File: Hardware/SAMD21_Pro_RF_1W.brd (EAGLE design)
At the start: 53.3 x 40.6 mm, 134 parts, among them J10 AVR_SPI_PROG_3X2TESTPOINTS, J12 5.5x2.1mm Barrel, J13 U.FL, J7 PTH, J9 External On/Off, Q1 310mA/60V/1.6Ω, U1 MCP73831, U3 3.3V, U4 ATSAMD21G, U5 4MB Flash, U6 E19-915MS1W, U7 ADJ5, U8 TXB0108DQSR, Y1 32.768kHz

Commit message: Finalizing things
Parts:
- moved U$26 121.9 mm to (-34.3, -14.0), flipped to the top
- moved FRAME2 81.3 mm to (-14.0, -12.7), flipped to the top
- moved U$29 51.6 mm to (52.5, 34.7), flipped to the top
- moved U$40 51.3 mm to (52.3, 0.38), flipped to the top
- moved FD2 50.8 mm to (52.1, 36.8), flipped to the bottom
- moved J7 50.8 mm to (1.27, 3.81), flipped to the top
- moved U6 50.8 mm to (1.27, 7.62), flipped to the bottom
- moved U$56 48.8 mm to (51.1, 0.89), flipped to the bottom
- moved U$54 48.5 mm to (50.9, 39.8), flipped to the bottom
- moved J13 48.3 mm to (50.8, 31.1), flipped to the top
- moved LOGO1 48.3 mm to (2.54, 36.7), flipped to the bottom
- moved U$35 48.3 mm to (50.8, 33.8), flipped to the bottom
- moved U$61 48.3 mm to (2.54, 36.7), flipped to the top
- moved U$81 47.8 mm to (50.5, 11.4), flipped to the top
- moved U$32 46.0 mm to (3.68, 5.59), flipped to the bottom
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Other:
- outline, holes or cut-outs redrawn

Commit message: x02
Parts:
- removed FRAME2: FRAME-LEDGER, SparkFun-Aesthetics:CREATIVE_COMMONS
- removed J15, J2: (no value), SparkFun-Connectors:1X04_1MM_RA
- removed LED1: RED, SparkFun-LED:LED-0603
- removed R15: 240, SparkFun-Resistors:0603
- removed R16: 10k, SparkFun-Resistors:0603
- removed S3: (no value), SparkFun-Switches:TACTILE_SWITCH_SMD_RIGHT_ANGLE
- removed U7: ADJ5, SparkFun-IC-Power:SOT223
- removed U8: TXB0108DQSR, SparkFun-IC-Comms:UFDFN-20
- added D2: Green, SparkFun-LED:LED-0603
- added FRAME1: FRAME-LEDGER, SparkFun-Aesthetics:CREATIVE_COMMONS
- added J14: CORTEX_DEBUG_PTH, SparkFun-Connectors:2X5-PTH-1.27MM
- added Q2: 310mA/60V/1.6Ω, SparkFun-DiscreteSemi:SOT323
- added R11: 10k, SparkFun-Resistors:0603
- added R3, R4: 1k, SparkFun-Resistors:0603
- added S2: Power, SparkFun-Switches:SWITCH_SPST_SMD_A
- added U$58: (no value), SparkX:SPARKX-MEDIUM
- added U$59: (no value), buzzard_labels:D130
- added U$60: (no value), buzzard_labels:SCK18
- added U2: 3.3V, SparkFun-IC-Power:SOT23-5
- C1: value 10uF -> 15pF; device SparkFun-Capacitors:EIA3216 -> SparkFun-Capacitors:0603
- C10: value 0.1uF -> 10uF; device SparkFun-Capacitors:0603 -> SparkFun-Capacitors:EIA3216
- C11, C14: value 0.1uF -> 1.0uF
- C12: value 1.0uF -> 10uF; device SparkFun-Capacitors:0603 -> SparkFun-Capacitors:EIA3216
- C13, C7: value 10uF -> 0.1uF; device SparkFun-Capacitors:EIA3216 -> SparkFun-Capacitors:0603
- C3: value 15pF -> 0.1uF
- C5: value 1.0uF -> 0.1uF
- C8: value 0.1uF -> 4.7uF
- C9: value 4.7uF -> 10uF; device SparkFun-Capacitors:0603 -> SparkFun-Capacitors:EIA3216
- D1: value Green -> Yellow
- D3: value 3A/10V/300mV -> BLUE; device SAMD21_ProRF_1W:SOD-323 -> SparkFun-LED:LED-0603
- D4: value BLUE -> 3A/10V/300mV; device SparkFun-LED:LED-0603 -> SAMD21_ProRF_1W:SOD-323
- D6: value Yellow -> RED
- J10: value AVR_SPI_PROG_3X2TESTPOINTS -> (none); device SparkFun-Connectors:2X3_TEST_POINTS -> SparkFun-Connectors:1X10_NO_SILK
- J11: device SparkFun-Connectors:1X09_NO_SILK -> SparkFun-Connectors:1X04_1MM_RA
- J12: value 5.5x2.1mm Barrel -> (none); device SparkFun-Connectors:POWER_JACK_SMD -> SparkFun-Connectors:1X01_NO_SILK
- J13: value U.FL -> (none); device SparkFun-Connectors:U.FL -> SparkFun-Connectors:1X04_1MM_RA
- J3: value (none) -> PTH; device SparkFun-Connectors:1X10_NO_SILK -> SparkFun-Connectors:1X02_NO_SILK
- J4: device SparkFun-Connectors:1X01_NO_SILK -> SparkFun-Connectors:1X02_NO_SILK
- J5: value (none) -> 5.5x2.1mm Barrel; device SparkFun-Connectors:1X09_NO_SILK -> SparkFun-Connectors:POWER_JACK_SMD
- J7: value PTH -> (none); device SparkFun-Connectors:1X02_NO_SILK -> SparkFun-Connectors:1X09_NO_SILK
- J8: value (none) -> External On/Off
- J9: value External On/Off -> (none); device SparkFun-Connectors:1X02_NO_SILK -> SparkFun-Connectors:1X09_NO_SILK
- R10, R7, R9: value 1k -> 10k
- R13: value 1k -> 2.2k
- R14: value 750 -> 2.2k
- R2, R8: value 10k -> 1k
- R5: value 2.2k -> 240
- R6: value 10k -> 750
- S1: value Power -> MOMENTARY-SWITCH-SPST-SMD-5.2-REDUNDANT; device SparkFun-Switches:SWITCH_SPST_SMD_A -> SparkFun-Switches:TACTILE_SWITCH_SMD_5.2MM
- U$10: device buzzard_labels (25):SCK10 -> buzzard_labels:MISO4
- U$18: device D2:D20 -> buzzard_labels:SCK5
- U$2: device D2:D20 -> buzzard_labels:MISO4
- U$20: device D3:D30 -> buzzard_labels:MOSI3
- U$21: device D3:D30 -> buzzard_labels:SPI11
- U$22: device D4:D40 -> buzzard_labels:MISO17
- U$26: value SPECIAL_INSTRUCTIONS-ORDERING -> (none); device SparkFun-Aesthetics:ORDERING_INSTRUCTIONS -> buzzard_labels:SAMD21_PRORF_1W5
- U$31: device D4:D40 -> buzzard_labels:MOSI16
- U$36: device buzzard_labels (25):RST2 -> buzzard_labels:OFF#ON1
- U$39: device buzzard_labels (28):ON#OFF0 -> buzzard_labels:SCK5
- U$65: device buzzard_labels (9):CHG1 -> buzzard_labels:SPI11
- U$8: device buzzard_labels (25):MISO8 -> buzzard_labels:SPI2
- U$9: device buzzard_labels (25):MOSI9 -> buzzard_labels:MOSI3
- U1: value MCP73831 -> ATSAMD21G; device SparkFun-IC-Power:SOT23-5 -> temp:QFN-48_NO_EXPOSED_PAD
- U3: value 3.3V -> ADJ5; device SparkFun-IC-Power:SOT23-5 -> SparkFun-IC-Power:SOT223
- U4: value ATSAMD21G -> 4MB Flash; device temp:QFN-48_NO_EXPOSED_PAD -> SparkFun-IC-Memory:SO08
- U5: value 4MB Flash -> E19-915MS1W; device SparkFun-IC-Memory:SO08 -> SAMD21_ProRF_1W:E19-915MS1W
- U6: value E19-915MS1W -> TXB0108DQSR; device SAMD21_ProRF_1W:E19-915MS1W -> SparkFun-IC-Comms:UFDFN-20
- moved U$26 56.9 mm to (2.79, 29.2), turned to 270 degrees
- moved S1 52.7 mm to (49.5, 34.8), flipped to the bottom, turned to 270 degrees
- moved J13 52.6 mm to (5.08, 5.08), flipped to the bottom, turned to 0 degrees
- moved U$29 51.6 mm to (0.89, 34.7), flipped to the bottom
- moved U$40 51.3 mm to (1.02, 0.38), flipped to the bottom
- moved U$56 48.8 mm to (2.29, 0.89), flipped to the top
- moved U$54 48.5 mm to (2.41, 39.8), flipped to the top
- moved U$35 48.3 mm to (2.54, 33.8), flipped to the top
- moved U$36 47.8 mm to (42.8, 4.70), flipped to the top
- moved U$81 47.8 mm to (2.79, 11.4), flipped to the bottom
- moved U$28 46.8 mm to (52.7, 33.3), flipped to the bottom, turned to 90 degrees
- moved U$32 46.0 mm to (49.7, 5.59), flipped to the top
- moved J7 45.8 mm to (33.0, 36.8), flipped to the bottom, turned to 0 degrees
- moved U$70 45.5 mm to (3.91, 6.92), flipped to the bottom
- moved U$72 45.5 mm to (3.91, 8.45), flipped to the bottom
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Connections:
- removed net CHARGE_STAT: R9.1, U1.1
- removed net D2: J3.6, U4.23
- removed net D3: J3.5, U4.14
- removed net D4: J3.4, U4.13
- removed net E19_RST: U4.26, U6.P$8
- removed net N$11: R5.1, U1.5
- removed net N$8: D4.C, R9.2
- removed net N$9: J9.2, S1.1
- removed net VBATT_LVL: R1.1, R2.2, U4.47
- new net !E19_RST: Q1.2, R9.1, U1.22
- new net !E19_RST5V: Q1.3, R11.1, U5.P$8
- new net D13: R4.2, U1.26
- new net EEPROM_MISO: J6.6, U1.23, U4.2
- new net EEPROM_MOSI: J6.4, U1.13, U4.5
- new net EEPROM_SCLK: J6.5, U1.14, U4.6
- new net N$3: D3.A, R4.1
- net !E19_CS: now also Q2.2, R10.1, U1.28; no longer Q1.2, R12.1, U4.28
- net !E19_CS5V: now also Q2.3, R12.1, U5.P$15; no longer Q1.3, R16.1, U6.P$15
- net !RST: now also J14.10, J6.8, R1.1, S1.3, S1.4, U1.40; no longer J10.5, J3.8, R6.1, S3.1, U4.40
- net 3.3V: now also C10.+, C11.1, C13.2, C5.2, D2.A, J11.2, J13.2, J14.1, J6.2, Q2.1, R1.2, R10.2, R14.2, R7.2, R9.2, U1.17, U1.36, U1.43, U1.44, U2.5, U4.3, U4.7, U4.8, U6.5, U6.6; no longer C10.2, C12.1, C13.+, C14.2, D6.A, J10.2, J15.2, J2.2, J3.2, R12.2, R6.2, U3.5, U4.17, U4.36, U4.43, U4.44, U5.3, U5.7, U5.8, U8.5, U8.6
- net 5V: now also C12.+, C14.1, C15.2, D4.C, R11.2, R12.2, U2.1, U2.3, U5.P$11, U6.16; no longer C5.1, C7.+, C8.2, D3.C, R16.2, U3.1, U3.3, U6.P$11, U8.16
- net A0: now also J7.9, U1.3; no longer J11.9, U4.3
- net A1: now also J7.8, U1.7; no longer J11.8, U4.7
- net A2: now also J7.7, U1.8; no longer J11.7, U4.8
- net A3: now also J7.6, U1.9; no longer J11.6, U4.9
- net A4: now also J7.5, U1.10; no longer J11.5, U4.10
- net ANT: now also J12.1, U5.P$19; no longer J13.FEED, J4.1, U6.P$19
- net D+: now also U1.34; no longer U4.34
- net D-: now also U1.33; no longer U4.33
- net D10: now also U1.27, U6.9; no longer U4.27, U8.9
- net D11: now also U1.25, U6.10; no longer U4.25, U8.10
- net D5: now also J6.7, U1.24; no longer J3.7, U4.24
- net D8_!FLASH_CS: now also R7.1, U1.11, U4.1; no longer R8.1, U4.11, U5.1
- net D9: now also J6.3, U1.12; no longer J3.3, U4.12
- net DIO05V: now also U5.P$7, U6.13; no longer U6.P$7, U8.13
- net DIO15V: now also U5.P$6, U6.12; no longer U6.P$6, U8.12
- net DIO25V: now also U5.P$5, U6.11; no longer U6.P$5, U8.11
- net E19_INT: now also U1.29, U6.8; no longer U4.29, U8.8
- net E19_RXEN: now also U1.38, U6.7; no longer U4.38, U8.7
- net E19_RXEN5V: now also U5.P$17, U6.14; no longer U6.P$17, U8.14
- net E19_TXEN: now also U1.37, U6.4; no longer U4.37, U8.4
- net E19_TXEN5V: now also U5.P$16, U6.17; no longer U6.P$16, U8.17
- net GND: now also C1.1, C10.-, C11.2, C12.-, C13.1, C14.2, C5.1, C7.1, C8.2, C9.-, D3.C, D6.C, J10.1, J10.10, J10.2, J10.3, J10.4, J10.5, J10.7, J10.8, J10.9, J14.3, J14.5, J3.1, J4.1, J5.GND, J5.P$4, J9.1, J9.2, J9.3, J9.4, J9.5, J9.6, J9.7, J9.8, J9.9, R6.1, S1.1, S1.2, U1.18, U1.35, U1.42, U1.5, U2.2, U4.4, U5.P$1, U5.P$10, U5.P$18, U5.P$20, U5.P$21, U5.P$22, U5.P$9, U6.15; no longer C1.-, C10.1, C11.1, C12.2, C13.-, C14.1, C5.2, C7.-, C8.1, C9.2, J12.GND, J12.P$4, J13.2, J15.1, J2.1, J5.1, J5.2, J5.3, J5.4, J5.5, J5.6, J5.7, J5.8, J5.9, J6.1, J6.10, J6.2, J6.3, J6.4, J6.5, J6.6, J6.7, J6.8, J6.9, J8.1, LED1.C, R14.1, R2.1, R5.2, S3.2, U1.2, U3.2, U4.18, U4.35, U4.42, U4.5, U5.4, U6.P$1, U6.P$10, U6.P$18, U6.P$20, U6.P$21, U6.P$22, U6.P$9, U8.15
- net MISO: now also J14.6, J7.2, U1.21, U6.2; no longer J10.1, J11.2, U4.21, U5.2, U8.2
- net MISO5V: now also U5.P$13, U6.19; no longer U6.P$13, U8.19
- net MOSI: now also J7.3, U1.19, U6.3; no longer J11.3, U4.19, U5.5, U8.3
- net MOSI5V: now also U5.P$14, U6.18; no longer U6.P$14, U8.18
- net N$1: now also D1.C, R2.2; no longer D6.C, R10.2
- net N$12: now also D4.A; no longer D3.A
- net N$13: now also R5.1, R6.2, U3.1; no longer R14.2, R15.1, U7.1
- net N$14: now also R5.2, U3.2, U3.4; no longer R15.2, U7.2, U7.4
- net N$2: now also D2.C, R3.2; no longer D1.C, R7.2
- net N$38: now also D6.A, R8.1; no longer LED1.A, R13.1
- net N$6: now also C1.2, U1.1; no longer C2.2, U4.1
- net N$7: now also C2.2, U1.2; no longer C3.2, U4.2
- net RAW: now also J6.1, J8.1, S2.2, U3.3; no longer J3.1, J9.1, S1.2, U7.3
- net RXI: now also J6.10, U1.16; no longer J3.10, U4.16
- net RX_LED: now also R2.1, U1.48; no longer R10.1, U4.48
- net SCK: now also J7.4, U1.20, U6.1; no longer J11.4, U4.20, U5.6, U8.1
- net SCK5V: now also U5.P$12, U6.20; no longer U6.P$12, U8.20
- net SCL: now also J11.4, J13.4, R14.1, U1.32; no longer J15.4, J2.4, U4.32
- net SDA: now also J11.3, J13.3, R13.1, U1.31; no longer J15.3, J2.3, U4.31
- net SWDCLK: now also J14.4, U1.45; no longer J10.3, U4.45
- net SWDIO: now also J14.2, U1.46; no longer J10.4, U4.46
- net TXO: now also J6.9, U1.15; no longer J3.9, U4.15
- net TX_LED: now also R3.1, U1.39; no longer R7.1, U4.39
- net USB_VCC: now also C3.2, C8.1, J4.2; no longer C11.2, C9.1, D4.A, J8.2, U1.4
- net VBATT: now also C9.+, J3.2, J5.VIN0, J8.2, S2.3; no longer C1.+, J12.VIN0, J7.2, R1.2, S1.3, U1.3
- net VDDANA: now also C7.2, U1.6; no longer C15.2, U4.6
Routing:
- net CHARGE_STAT: track 74.0 -> 0.00 mm, vias 4 -> 0
- net VBATT_LVL: track 52.4 -> 0.00 mm, vias 6 -> 0
- net USB_VCC: track 100.4 -> 53.3 mm, vias 6 -> 4
- net !E19_RST5V: track 0.00 -> 45.1 mm, vias 0 -> 3
- net E19_RST: track 32.0 -> 0.00 mm, vias 1 -> 0
- net EEPROM_MISO: track 0.00 -> 30.0 mm, vias 0 -> 2
- net MOSI: track 71.8 -> 50.4 mm, vias 4 -> 2
- net EEPROM_SCLK: track 0.00 -> 20.8 mm, vias 0 -> 1
- net EEPROM_MOSI: track 0.00 -> 19.3 mm, vias 0 -> 1
- net !E19_RST: track 0.00 -> 18.0 mm, vias 0 -> 2
- net SCK: track 69.6 -> 52.3 mm, vias 7 -> 4
- net 3.3V: track 187.3 -> 204.5 mm
- net D4: track 14.2 -> 0.00 mm, vias 1 -> 0
- net D13: track 0.00 -> 13.8 mm, vias 0 -> 2
- net D3: track 13.5 -> 0.00 mm, vias 1 -> 0
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- removed copper zone on layer 16, net ANT
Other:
- outline, holes or cut-outs redrawn
- board text added: "x02"
- board text removed: "0.8mm Board Thickness"
- board text removed: "x01"

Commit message: x02 ready for order
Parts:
- removed LOGO1: OSHW-LOGOMINI, SparkFun-Aesthetics:OSHW-LOGO-MINI
- removed U$29, U$40, U$54, U$56: (no value), Labels:QWIIC-TEXT-04
- added U$64, U$67: (no value), Labels:QWIIC_COPYRIGHT_SMALL
- U$30: device Labels:QWIIC-LOGO-MEDIUM -> Labels:QWIIC_COPYRIGHT_MEDIUM
- U$34: value SPARKX-LOGO2 -> SPARKX-LOGO4; device SparkX:SPARKX-TINY -> SparkX:SPARKX-MEDIUM
- U$51: device SparkX:SPARKX-MEDIUM -> Labels:QWIIC_COPYRIGHT_MEDIUM
- moved FRAME1 81.3 mm to (-14.0, -12.7), flipped to the top
- moved U$28 52.1 mm to (0.64, 33.3), flipped to the top
- moved FD1 50.8 mm to (52.1, 36.8), flipped to the bottom
- moved J3 50.8 mm to (1.27, 3.81), flipped to the top
- moved U5 50.8 mm to (1.27, 7.62), flipped to the bottom
- moved FD2 49.8 mm to (1.78, 2.29), flipped to the top
- moved FD3 49.8 mm to (1.78, 2.29), flipped to the bottom
- moved U$35 48.3 mm to (50.8, 33.8), flipped to the bottom
- moved U$26 47.8 mm to (50.5, 29.2), flipped to the bottom
- moved U$81 47.8 mm to (50.5, 11.4), flipped to the top
- moved U$32 46.0 mm to (3.68, 5.59), flipped to the bottom
- moved S1 45.7 mm to (3.81, 34.8), flipped to the top
- moved U$63 45.7 mm to (49.5, 11.5), flipped to the top
- moved U$59 45.6 mm to (49.5, 9.96), flipped to the top
- moved U$70 45.5 mm to (49.4, 6.92), flipped to the top
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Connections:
- net GND: now also J14.9
- net MISO: no longer J14.6
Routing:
- net MISO: track 77.3 -> 53.4 mm, vias 5 -> 2
- net GND: track 133.4 -> 132.6 mm
- net 3.3V: track 204.5 -> 203.9 mm
- added copper zone on layer 16, net ANT
- removed copper zone on layer 1, net ANT
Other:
- outline, holes or cut-outs redrawn

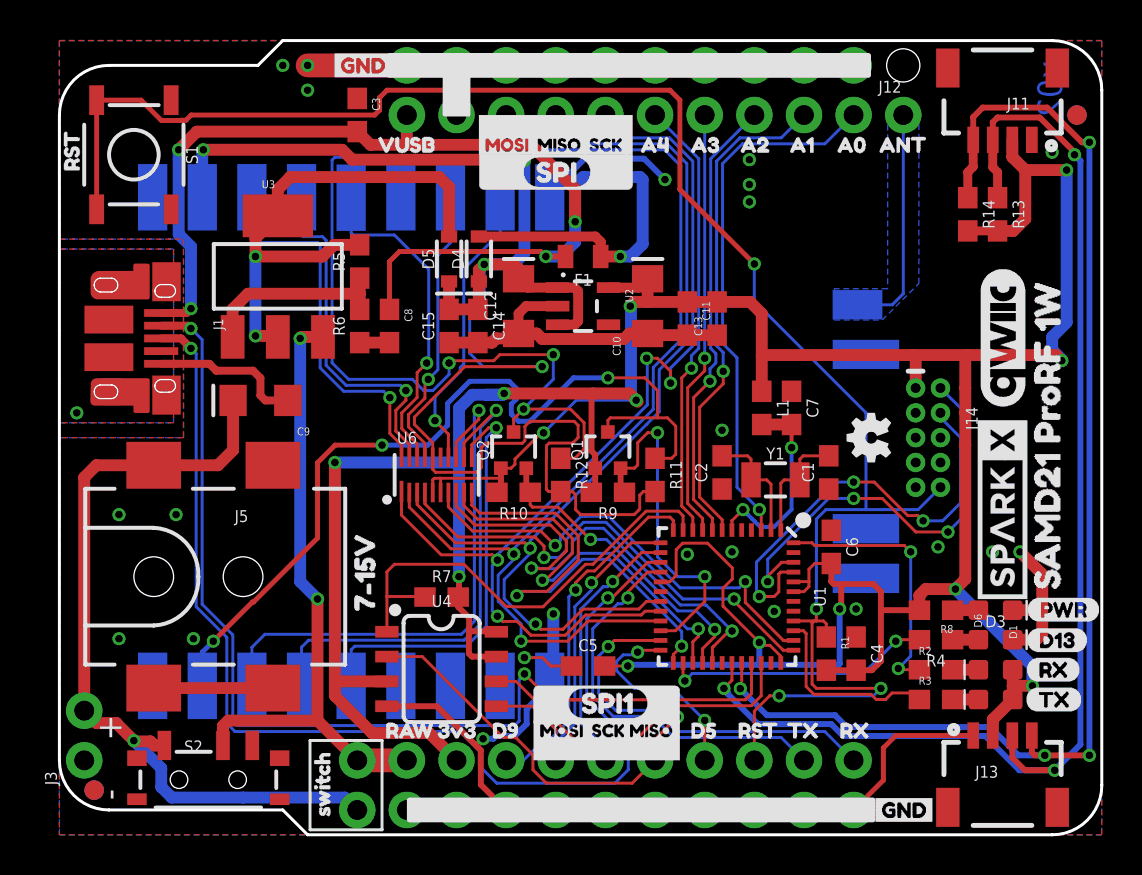
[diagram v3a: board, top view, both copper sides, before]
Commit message: Brought libraries into spec
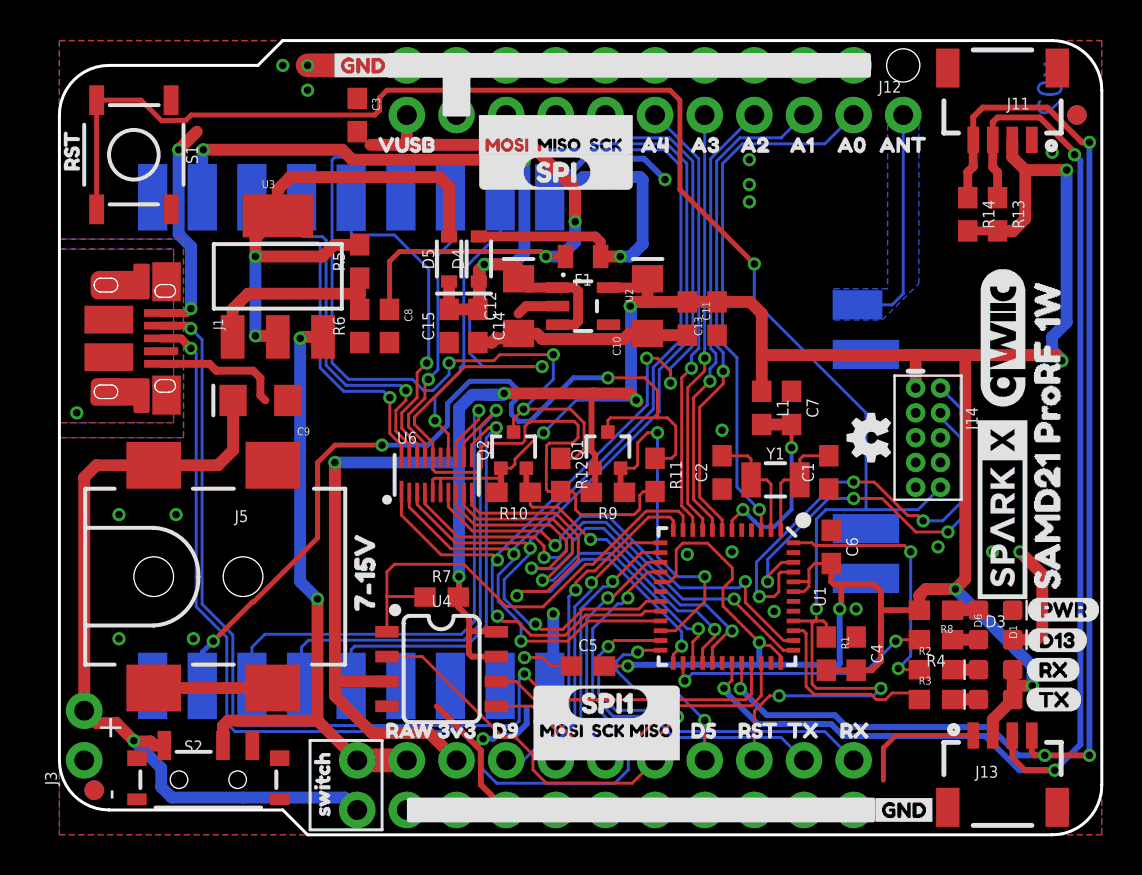
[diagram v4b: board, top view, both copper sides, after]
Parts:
- D4, D5: value 3A/10V/300mV -> 3A/10V/280mV; device SAMD21_ProRF_1W:SOD-323 -> SparkFun-DiscreteSemi:SOD-323
- U1: device temp:QFN-48_NO_EXPOSED_PAD -> SparkFun-IC-Microcontroller:QFN-48_NO_EXPOSED_PAD
- U5: value E19-915MS1W -> (none); device SAMD21_ProRF_1W:E19-915MS1W -> SparkFun-RF:E19-915MS1W
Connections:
- new net V_USB: C3.2
- net USB_VCC: no longer C3.2
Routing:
- net GND: track 132.6 -> 111.6 mm
- net USB_VCC: track 53.3 -> 44.1 mm
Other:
- board text added: "BAT60A"
- board text added: "Ferrite Chip 30 Ohm"
- board text added: "N-ch"
- board text added: "Tall Cap Tactile"

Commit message: Fixes
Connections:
- removed net USB_VCC: C8.1, F1.2, J1.VBUS, J4.2, JP1.2
- net V_USB: now also C8.1, F1.2, J1.VBUS, J4.2, JP1.2
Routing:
- net V_USB: track 0.00 -> 53.3 mm, vias 0 -> 4
- net USB_VCC: track 44.1 -> 0.00 mm, vias 4 -> 0
- net GND: track 111.6 -> 101.4 mm

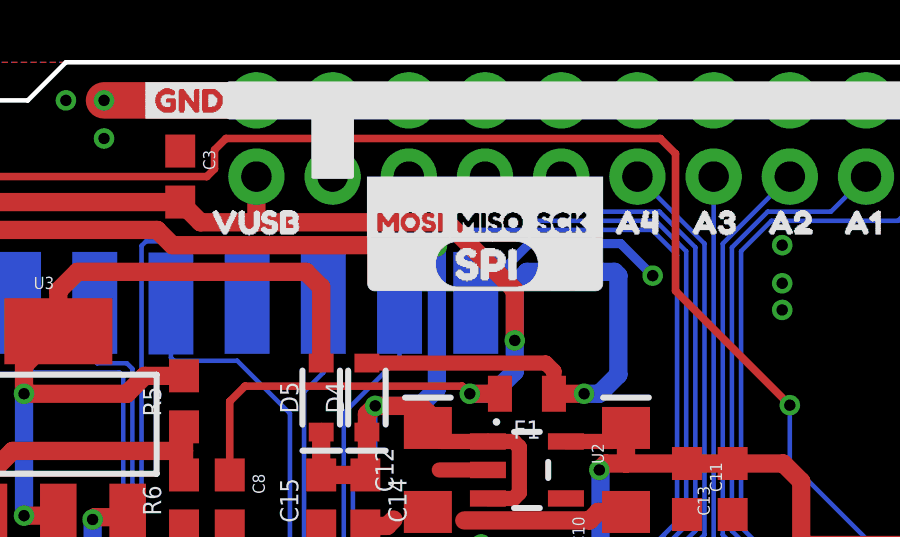
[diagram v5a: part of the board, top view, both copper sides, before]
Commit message: Fixed silkscreen of "SPI" on top side
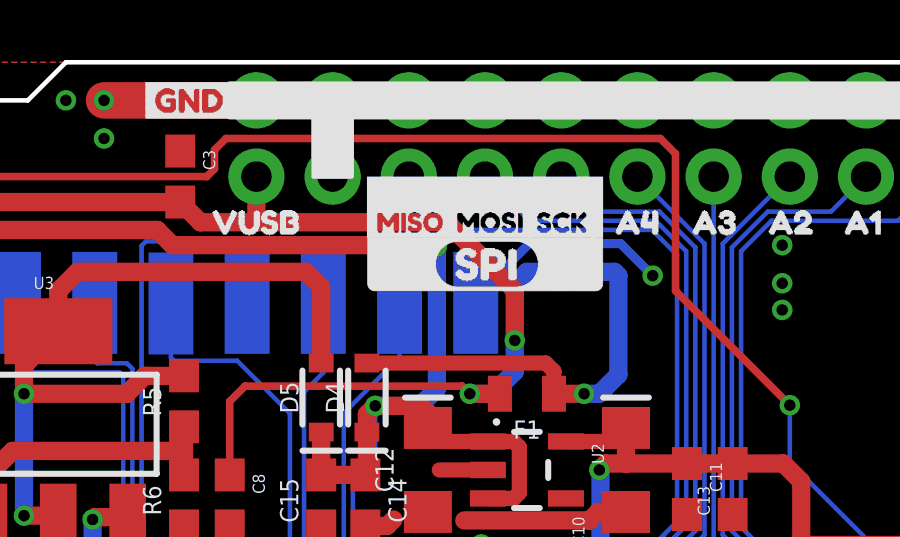
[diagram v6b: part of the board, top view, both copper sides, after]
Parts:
- moved U$10 2.67 mm to (21.2, 35.3)
- moved U$9 2.67 mm to (23.9, 35.3)
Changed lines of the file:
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@@
 <attribute name="VALUE" value="Yellow" x="46.2534" y="13.6525" size="0.508" layer="27" ratio="15" rot="R180"/>
 </element>
-<element name="FRAME1" library="SparkFun-Aesthetics" package="CREATIVE_COMMONS" value="FRAME-LEDGER" x="-13.97" y="-12.7"/>
+<element name="FRAME1" library="SparkFun-Aesthetics" package="CREATIVE_COMMONS" value="FRAME-LEDGER" x="-13.97" y="-12.7">
+<attribute name="DESIGNER" value="" x="-13.97" y="-12.7" size="1.778" layer="27" display="off"/>
+<attribute name="REV" value="" x="-13.97" y="-12.7" size="1.778" layer="27" display="off"/>
+</element>
 <element name="J1" library="SparkFun-Connectors" package="USB-MICROB-PTH-MILL" value="" x="5.207" y="25.4" smashed="yes" rot="R270">
 <attribute name="NAME" x="7.874" y="26.416" size="0.508" layer="25" font="vector" rot="R270"/>
@@
 <element name="F1" library="SparkFun-Fuses" package="0805" value="6V 0.5A" x="26.797" y="29.591" smashed="yes" rot="R180">
 <attribute name="NAME" x="26.797" y="28.702" size="0.6096" layer="25" font="vector" ratio="20" rot="R180" align="bottom-center"/>
-<attribute name="VALUE" x="26.924" y="31.115" size="0.6096" layer="27" font="vector" ratio="20" align="top-center"/>
+<attribute name="PROD_ID" value="13945" x="26.797" y="29.591" size="1.778" layer="27" rot="R180" display="off"/>
+<attribute name="VALUE" value="6V 0.5A" x="26.924" y="31.115" size="0.6096" layer="27" font="vector" ratio="20" align="top-center"/>
 </element>
 <element name="R6" library="SparkFun-Resistors" package="0603" value="750" x="15.367" y="26.035" smashed="yes" rot="R90">
@@
 <element name="U$36" library="buzzard_labels" package="OFF#ON1" value="" x="10.541" y="4.699" rot="MR0"/>
 <element name="U$8" library="buzzard_labels" package="SPI2" value="" x="23.495" y="33.909" smashed="yes"/>
-<element name="U$9" library="buzzard_labels" package="MOSI3" value="" x="21.209" y="35.306" smashed="yes"/>
-<element name="U$10" library="buzzard_labels" package="MISO4" value="" x="23.876" y="35.306" smashed="yes"/>
+<element name="U$9" library="buzzard_labels" package="MOSI3" value="" x="23.876" y="35.306" smashed="yes"/>
+<element name="U$10" library="buzzard_labels" package="MISO4" value="" x="21.209" y="35.306" smashed="yes"/>
 <element name="U$39" library="buzzard_labels" package="SCK5" value="" x="26.543" y="35.306" smashed="yes"/>
 <element name="U$2" library="buzzard_labels" package="MISO4" value="" x="28.575" y="5.334" smashed="yes"/>
